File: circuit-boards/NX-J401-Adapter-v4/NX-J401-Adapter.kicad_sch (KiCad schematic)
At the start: 12 parts, among them J1 18V_OUT, J2 NX-BUTTON, J3 CONSOLE, J4 Power, SW1 RESET, SW2 RECOVERY

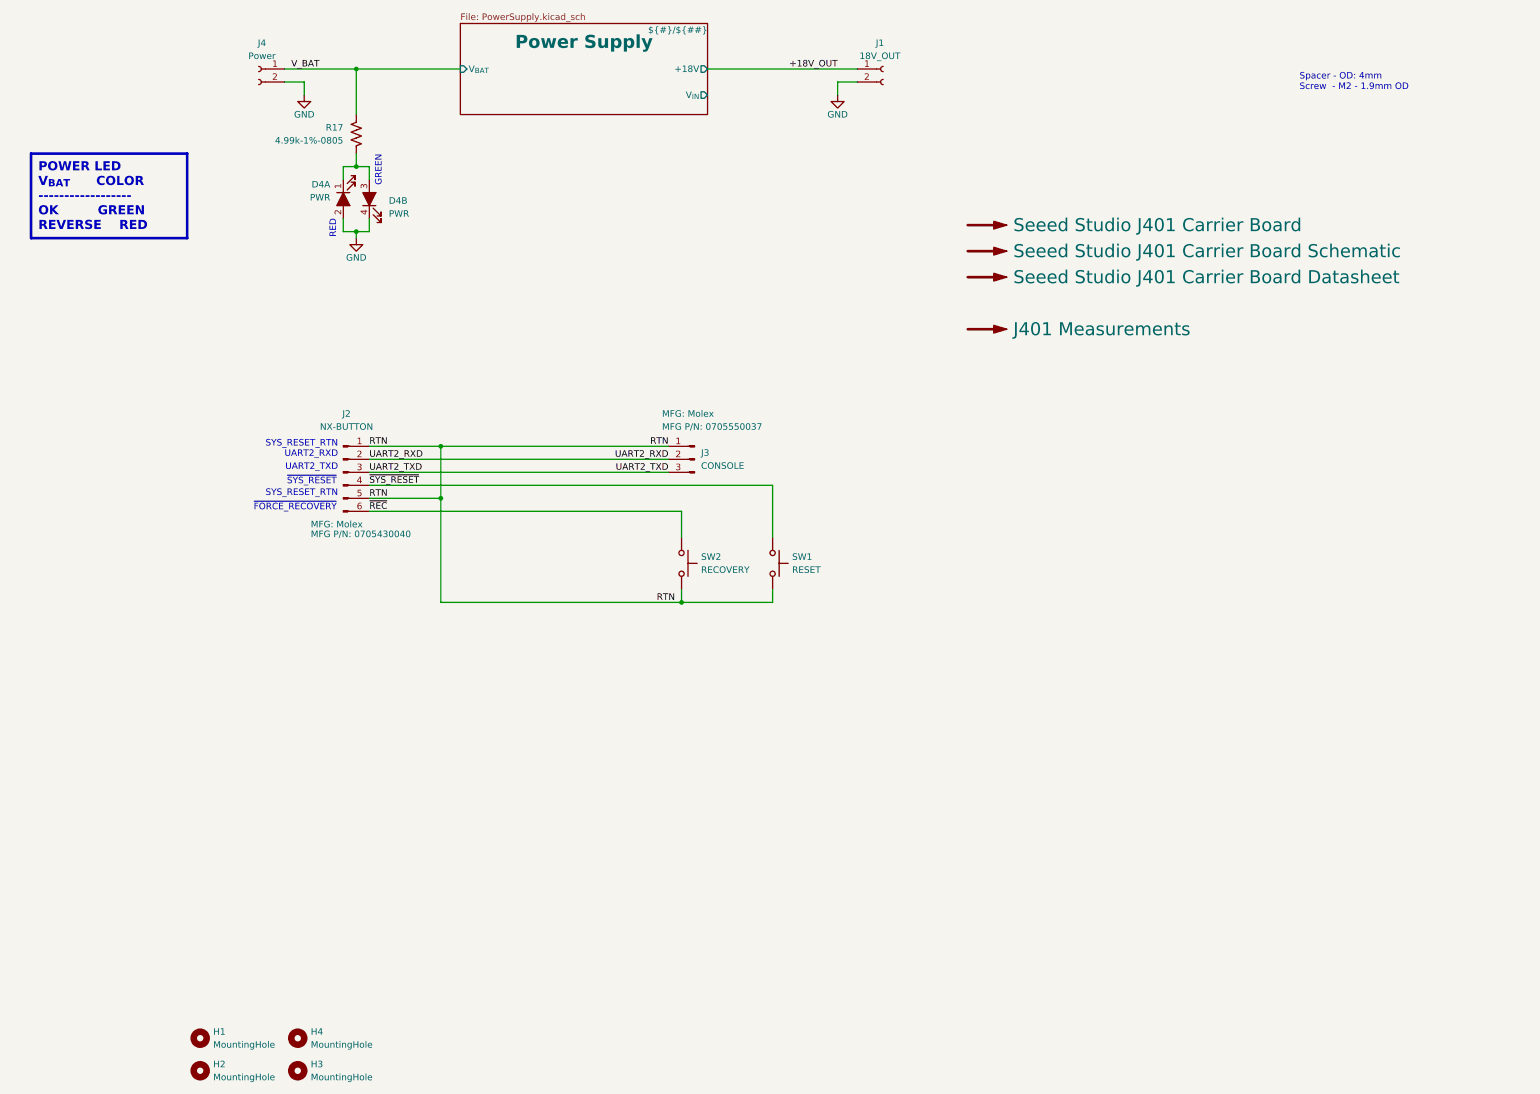
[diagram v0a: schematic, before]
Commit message: Update NX J401 Adapter to add PC LED and swap buttons
Signed-off-by: Scott Berman <sgberman1@gmail.com>
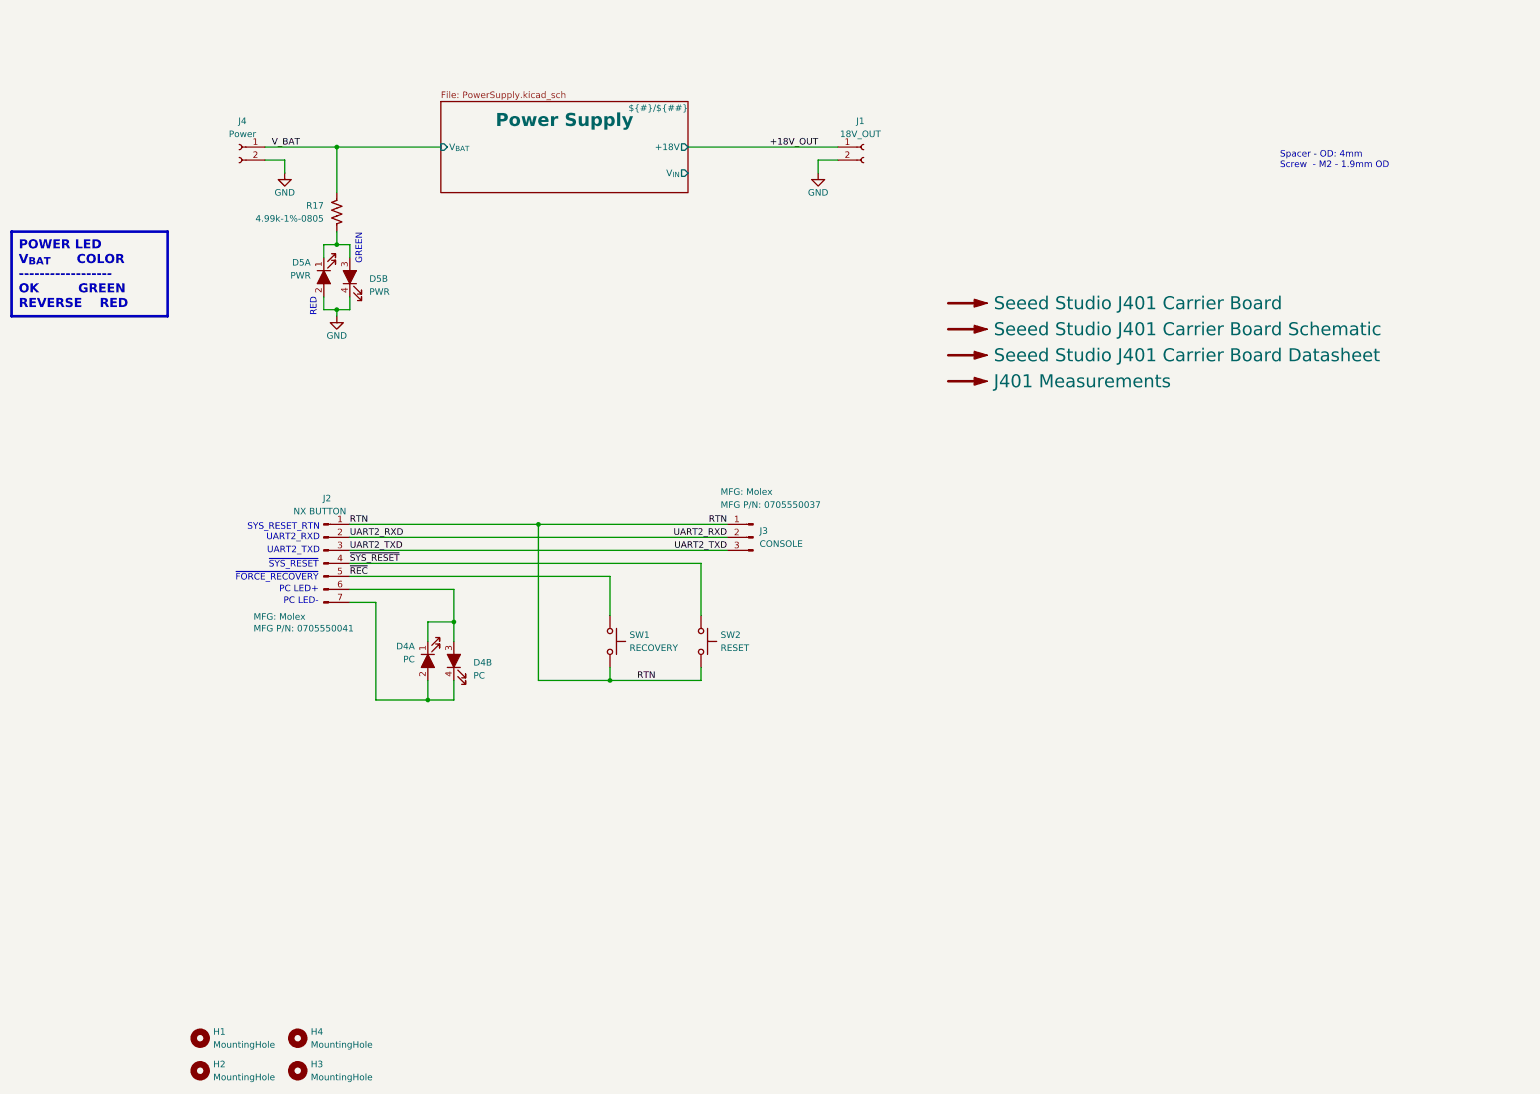
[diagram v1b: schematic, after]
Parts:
- removed J2: NX-BUTTON, NX-J401-Adapter:70555-0005, symbol Connector:Conn_01x06_Pin
- added D4: PC, NX-J401-Adapter:LED-Dialight-5913001858F, symbol NX-AdapterBoard:Dialight-Dual-LED
- added J2: NX BUTTON, NX-J401-Adapter:70555-0006, symbol Connector:Conn_01x07_Pin
- renumbered D4 to D5, SW2 to SW1, SW1 to SW2
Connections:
- net RTN: now also J2.1 (Pin_1)
- net UART2_RXD: now also J2.2 (Pin_2)
- net UART2_TXD: now also J2.3 (Pin_3)
- net ~{REC}: now also J2.5 (Pin_5)
- net ~{SYS_RESET}: now also J2.4 (Pin_4)
- new net: D4.1 (Red-K), D4.3 (Green-A), J2.6 (Pin_6)
- new net: D4.2 (RedA), D4.4 (Green-K), J2.7 (Pin_7)
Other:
- note added: "PC LED+"
- note added: "PC LED-"
- moved on the sheet: D5A, D5B, J1, J3, J4, R17, SW1, SW2

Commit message: Update NX-J401 and NX Button Interface boards
Signed-off-by: Scott Berman <scott.berman@bluerivertech.com>
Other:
- sheet Power Supply ports: added none; removed V_{IN}
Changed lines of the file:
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@@
 	(label "~{REC}"
 		(at 163.83 157.48 0)
-		(fields_autoplaced yes)
 		(effects
 			(font
@@
 	(label "RTN"
 		(at 237.49 147.32 180)
-		(fields_autoplaced yes)
 		(effects
 			(font
@@
 	(label "UART2_TXD"
 		(at 237.49 152.4 180)
-		(fields_autoplaced yes)
 		(effects
 			(font
@@
 	(label "RTN"
 		(at 223.52 177.8 180)
-		(fields_autoplaced yes)
 		(effects
 			(font
@@
 	(label "UART2_RXD"
 		(at 237.49 149.86 180)
-		(fields_autoplaced yes)
 		(effects
 			(font
@@
 	(label "UART2_TXD"
 		(at 163.83 152.4 0)
-		(fields_autoplaced yes)
 		(effects
 			(font
@@
 	(label "RTN"
 		(at 163.83 147.32 0)
-		(fields_autoplaced yes)
 		(effects
 			(font
@@
 	(label "V_BAT"
 		(at 148.59 73.66 0)
-		(fields_autoplaced yes)
 		(effects
 			(font
@@
 	(label "UART2_RXD"
 		(at 163.83 149.86 0)
-		(fields_autoplaced yes)
 		(effects
 			(font
@@
 	(label "+18V_OUT"
 		(at 255.27 73.66 180)
-		(fields_autoplaced yes)
 		(effects
 			(font
@@
 	(label "~{SYS_RESET}"
 		(at 163.83 154.94 0)
-		(fields_autoplaced yes)
 		(effects
 			(font
@@
 			(effects
 				(font
-					(size 1.27 1.27)
-				)
-				(justify right)
-			)
-		)
-		(pin "V_{IN}" output
-			(at 229.87 78.74 0)
-			(effects
-				(font
